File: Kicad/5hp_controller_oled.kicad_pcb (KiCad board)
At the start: 4 copper layers, 25 x 105 mm, 14 parts, among them J1 SSD1306, J2 AS5600_2_PWR, J4 AS5600_2_PWR, J5 AS5600_2_PWR

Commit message: Final pcb and frontpanel
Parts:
- moved J1 1.00 mm to (25.0, -41.8)
- moved BTN1 0.11 mm to (22.4, 45.2)
- moved BTN2 0.11 mm to (27.5, 45.2)
- moved LED1 0.11 mm to (16.4, 45.2)
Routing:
- net BTN2: track 71.9 -> 72.6 mm
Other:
- copper layers 4 -> 2
- board text added: "+3.3V"

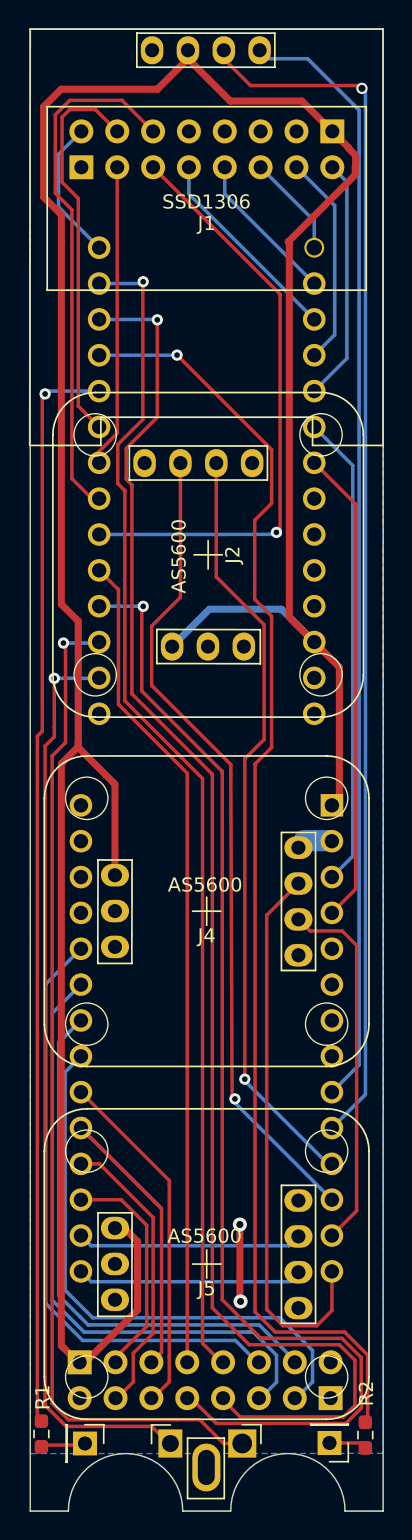
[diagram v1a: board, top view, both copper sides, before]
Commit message: Fixed pcb errors (wrong footprint TCA, freed up pin 13)
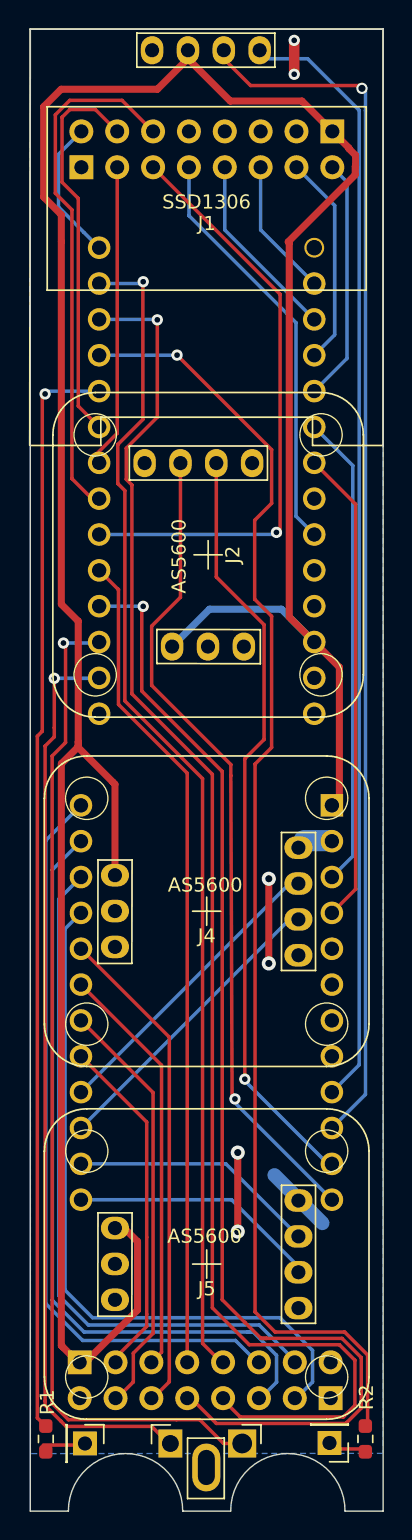
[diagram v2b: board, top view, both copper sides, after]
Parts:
- IC1: renamed from TCA9548; footprint SSD1306:DIP-28_W17.48mm_Socket -> SSD1306:DIP-24_W9.xx mm_Socket
- J10: renamed from To Board without MUX
- J16: renamed from To Board with Mux
- U1: renamed from Teensy 4.0
- moved R1 0.47 mm to (13.6, 44.9)
- moved R2 0.27 mm to (36.2, 44.9)
- renumbered BTN1 to J3, LED1 to J6, BTN2 to J7, LED2 to J9
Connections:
- J4 pad SCL: SC2 -> SC3
- J4 pad SDA: SD2 -> SD3
- J5 pad SCL: SC3 -> SC2
- J5 pad SDA: SD3 -> SD2
- U1 pad 20: LED8 -> unconnected-(U1-13_SCK_CRX1_LED-Pad20)
- U1 pad 21: LED7 -> LED8
- U1 pad 22: LED6 -> LED7
- U1 pad 28: unconnected-(U1-21_A7_RX5_BCLK1-Pad28) -> LED6
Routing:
- net SC2: track 39.4 -> 17.5 mm
- net LED6: track 14.5 -> 29.7 mm
- net GND: track 7.31 -> 19.6 mm, vias 2 -> 6
- net SD7: track 44.6 -> 54.7 mm
- net SC7: track 43.0 -> 53.2 mm
- net SC6: track 39.1 -> 49.3 mm
- net SC5: track 24.9 -> 35.0 mm
- net SD6: track 40.4 -> 50.5 mm
- net SC4: track 20.7 -> 30.1 mm
- net SD2: track 26.2 -> 17.4 mm
- net SD4: track 16.2 -> 24.6 mm
- net SD3: track 15.9 -> 21.5 mm
- net SC3: track 16.0 -> 21.5 mm
- net LED7: track 10.9 -> 13.4 mm
- net LED8: track 7.27 -> 9.81 mm
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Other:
- board text added: "m4live ctrl v1.1"
- board text removed: "m4live ctrl v1.0"
